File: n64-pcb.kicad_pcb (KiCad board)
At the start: 4 copper layers, 41 x 33.1 mm, 4 parts

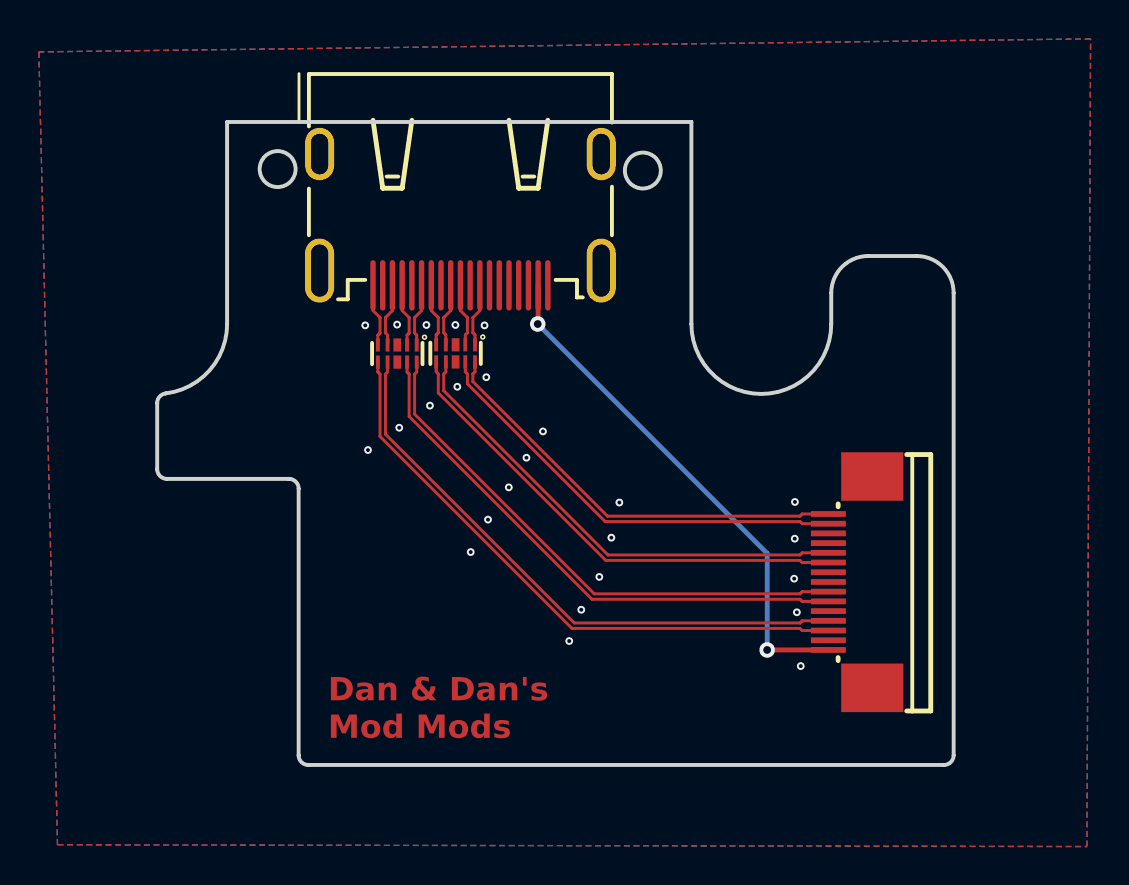
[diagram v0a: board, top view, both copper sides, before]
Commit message: diff pair length matching
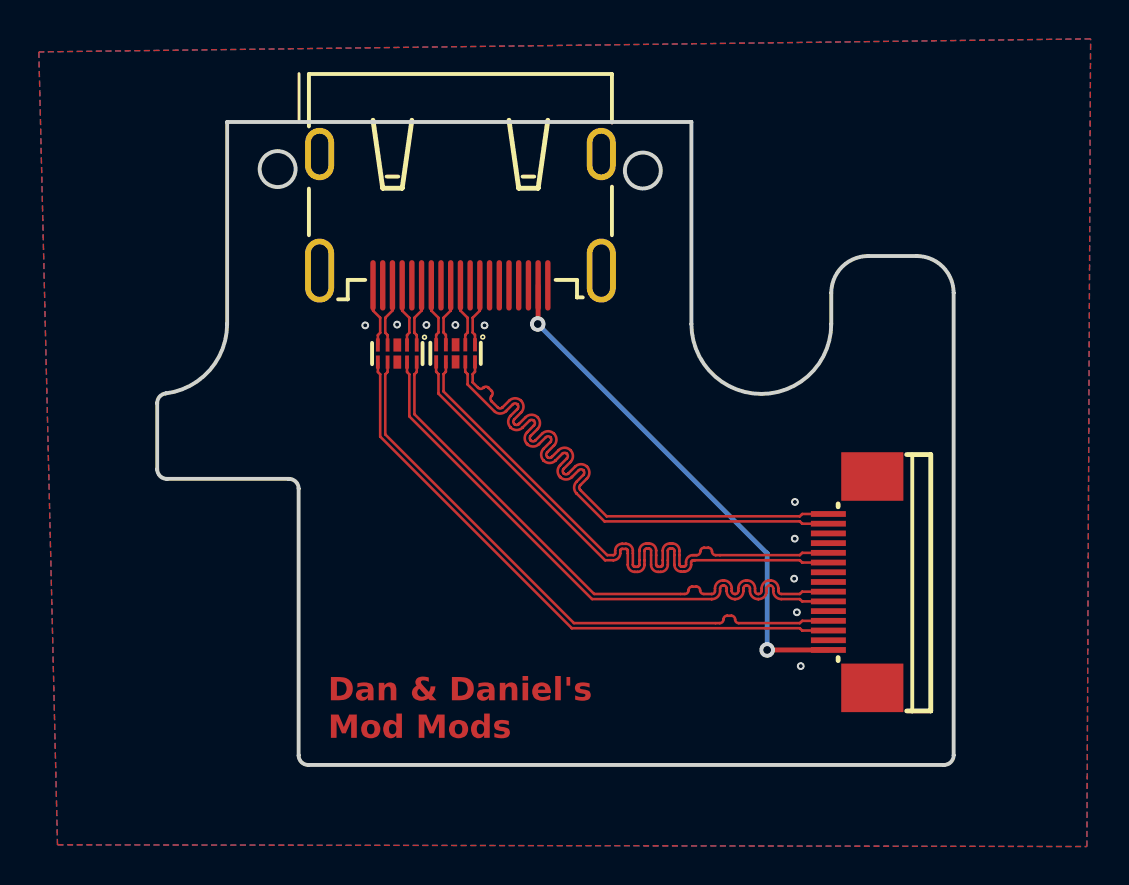
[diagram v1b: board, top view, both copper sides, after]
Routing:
- net /ESD_CLOCK-: track 22.3 -> 30.8 mm
- net /ESD_CLOCK+: track 22.7 -> 30.9 mm
- net /ESD_D0-: track 24.9 -> 30.9 mm
- net /ESD_D0+: track 25.3 -> 31.0 mm
- net /ESD_D1-: track 27.9 -> 30.9 mm
- net /ESD_D1+: track 28.4 -> 31.0 mm
- net GND: vias 25 -> 10
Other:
- board text added: "Dan & Daniel's Mod Mods"
- board text removed: "Dan & Dan's Mod Mods"
